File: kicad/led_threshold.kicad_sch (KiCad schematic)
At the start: 16 parts, among them Q1 2N7002E, Q2 2N7002E, SW5 EG6100-ND, U21 OPA189, U22 4x Comparator

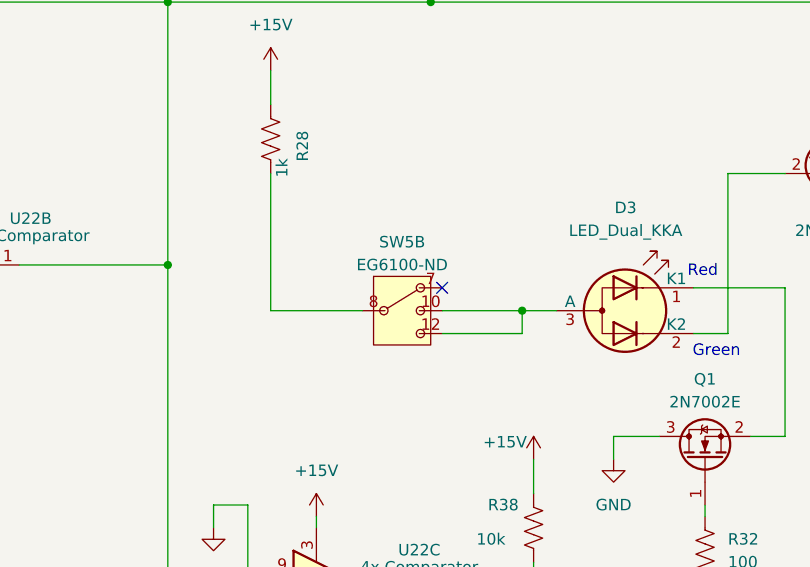
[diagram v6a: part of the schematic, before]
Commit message: Rearranged Edge Componenets, simpler board, wider but shorter depth
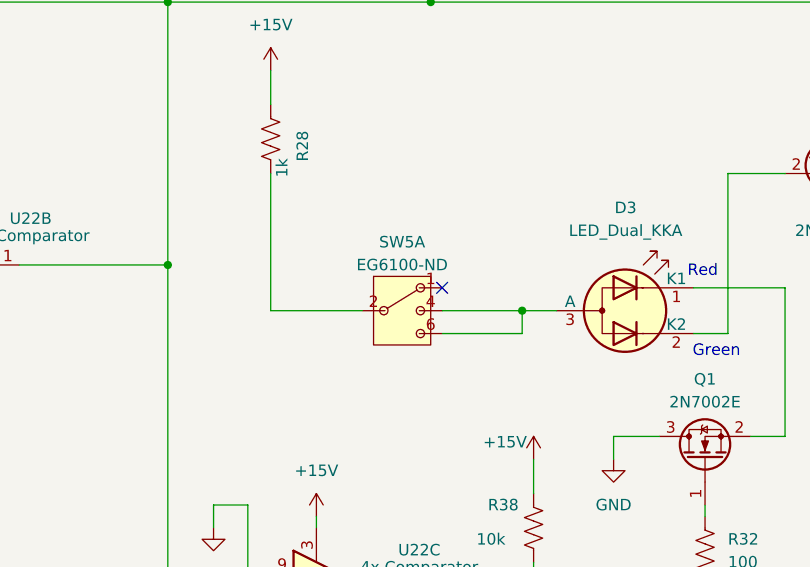
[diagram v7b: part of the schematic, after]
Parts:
- removed unit 2 of SW5
- added unit 1 of SW5
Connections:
- net at D3.3 (A): now also SW5.4, SW5.6
- net at R28.2: now also SW5.2
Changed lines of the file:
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@@
+	)
+	(symbol
+		(lib_id "Custom_Symbols:DP3T_1")
+		(at 180.34 66.04 0)
+		(unit 1)
+		(exclude_from_sim no)
+		(in_bom yes)
+		(on_board yes)
+		(dnp no)
+		(fields_autoplaced yes)
+		(property "Reference" "SW5"
+			(at 180.975 58.42 0)
+			(effects
+				(font
+					(size 1.27 1.27)
+				)
+			)
+		)
+		(property "Value" "EG6100-ND"
+			(at 180.975 60.96 0)
+			(effects
+				(font
+					(size 1.27 1.27)
+				)
+			)
+		)
+		(property "Footprint" "Custom_Footprints:Right Angle 3PDT Switch"
+			(at 180.34 66.04 0)
+			(effects
+				(font
+					(size 1.27 1.27)
+				)
+				(hide yes)
+			)
+		)
+		(property "Datasheet" ""
+			(at 180.34 66.04 0)
+			(effects
+				(font
+					(size 1.27 1.27)
+				)
+				(hide yes)
+			)
+		)
+		(property "Description" ""
+			(at 180.34 66.04 0)
+			(effects
+				(font
+					(size 1.27 1.27)
+				)
+				(hide yes)
+			)
+		)
+		(property "DIGIKEY" "EG6100-ND"
+			(at 180.34 66.04 0)
+			(effects
+				(font
+					(size 1.27 1.27)
+				)
+				(hide yes)
+			)
+		)
+		(property "PARTNO" "1004P6T1B4M7RE"
+			(at 180.34 66.04 0)
+			(effects
+				(font
+					(size 1.27 1.27)
+				)
+				(hide yes)
+			)
+		)
+		(property "MPN" ""
+			(at 180.34 66.04 0)
+			(effects
+				(font
+					(size 1.27 1.27)
+				)
+				(hide yes)
+			)
+		)
+		(pin "9"
+		)
+		(pin "10"
+		)
+		(pin "3"
+		)
+		(pin "5"
+		)
+		(pin "12"
+		)
+		(pin "8"
+		)
+		(pin "11"
+		)
+		(pin "7"
+		)
+		(pin "13"
+		)
+		(pin "6"
+		)
+		(pin "2"
+		)
+		(pin "4"
+		)
+		(pin "1"
+		)
+		(instances
+			(project "intensity_pi"
+				(path "/3a3d7bcb-6fa5-41ef-9ea1-6d4ab7c492fd/0e4e37c0-2fc7-4de2-ba74-9d178da3762c"
+					(reference "SW5")
+					(unit 1)
+				)
+			)
+		)
 	)
 	(symbol
@@
 				)
 			)
-		)
-	)
-	(symbol
-		(lib_id "Custom_Symbols:DP3T_1")
-		(at 180.34 66.04 0)
-		(unit 2)
-		(exclude_from_sim no)
-		(in_bom yes)
-		(on_board yes)
-		(dnp no)
-		(fields_autoplaced yes)
-		(property "Reference" "SW5"
-			(at 180.975 58.42 0)
-			(effects
-				(font
-					(size 1.27 1.27)
-				)
-			)
-		)
-		(property "Value" "EG6100-ND"
-			(at 180.975 60.96 0)
-			(effects
-				(font
-					(size 1.27 1.27)
-				)
-			)
-		)
-		(property "Footprint" "Custom_Footprints:Right Angle 3PDT Switch"
-			(at 180.34 66.04 0)
-			(effects
-				(font
-					(size 1.27 1.27)
-				)
-				(hide yes)
-			)
-		)
-		(property "Datasheet" ""
-			(at 180.34 66.04 0)
-			(effects
-				(font
-					(size 1.27 1.27)
-				)
-				(hide yes)
-			)
-		)
-		(property "Description" ""
-			(at 180.34 66.04 0)
-			(effects
-				(font
-					(size 1.27 1.27)
-				)
-				(hide yes)
-			)
-		)
-		(property "DIGIKEY" "EG6100-ND"
-			(at 180.34 66.04 0)
-			(effects
-				(font
-					(size 1.27 1.27)
-				)
-				(hide yes)
-			)
-		)
-		(property "PARTNO" "1004P6T1B4M7RE"
-			(at 180.34 66.04 0)
-			(effects
-				(font
-					(size 1.27 1.27)
-				)
-				(hide yes)
-			)
-		)
-		(property "MPN" ""
-			(at 180.34 66.04 0)
-			(effects
-				(font
-					(size 1.27 1.27)
-				)
-				(hide yes)
-			)
-		)
-		(pin "9"
-		)
-		(pin "10"
-		)
-		(pin "3"
-		)
-		(pin "5"
-		)
-		(pin "12"
-		)
-		(pin "8"
-		)
-		(pin "11"
-		)
-		(pin "7"
-		)
-		(pin "13"
-		)
-		(pin "6"
-		)
-		(pin "2"
-		)
-		(pin "4"
-		)
-		(pin "1"
-		)
-		(instances
-			(project ""
-				(path "/3a3d7bcb-6fa5-41ef-9ea1-6d4ab7c492fd/0e4e37c0-2fc7-4de2-ba74-9d178da3762c"
-					(reference "SW5")
-					(unit 2)
-				)
-			)
